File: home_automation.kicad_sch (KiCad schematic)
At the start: 44 parts, among them J1 AC In, J2 NodeMCU Header, J3 NodeMCU Header, J4 Conn_01x03_Male, J5 DHT11, J6 Conn_01x03_Male, J7 Conn_01x03_Male, J8 Conn_01x03_Male, K1 Relay_SPDT, K2 Relay_SPDT, K3 Relay_SPDT, K4 Relay_SPDT, Q1 D882_NPN_transistor, Q2 D882_NPN_transistor, Q3 D882_NPN_transistor, Q4 D882_NPN_transistor, U1 PC817, U2 PC817, U3 LM7805_TO220, U4 PC817, U5 PC817, U6 NodeMCU

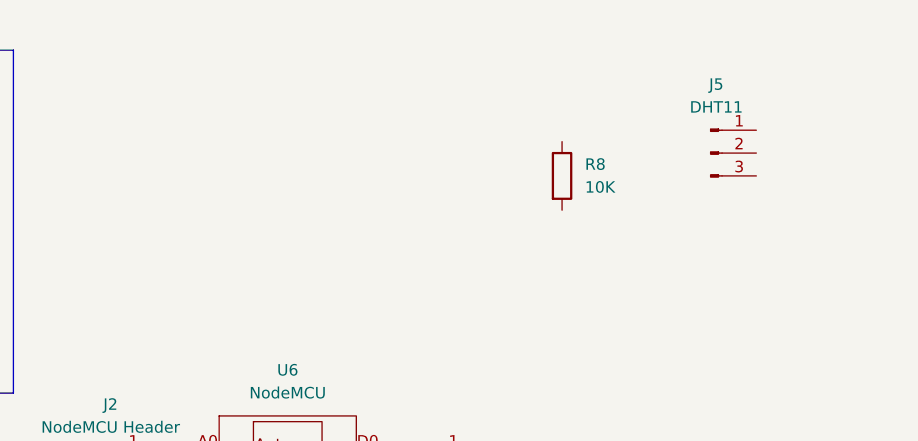
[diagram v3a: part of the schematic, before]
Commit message: DHT11 to NodeMCU  Wiring Completed
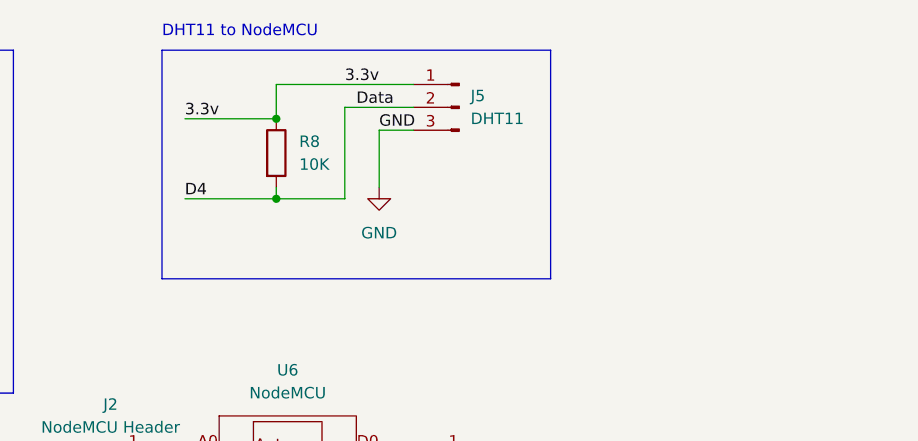
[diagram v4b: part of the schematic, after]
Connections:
- net GND: now also J5.3 (Pin_3)
- net 3.3v: now reaches J5.1 (Pin_1)
- net 3.3v: now also R8.1
- net D4: now reaches J5.2 (Pin_2)
- net D4: now also R8.2
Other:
- note added: "DHT11 to NodeMCU"
- moved on the sheet: J5, R8
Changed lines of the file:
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@@
     (rev "v1")
   )
+  (junction (at 203.2 25.4) (diameter 0) (color 0 0 0 0)
+  )
+  (junction (at 203.2 34.29) (diameter 0) (color 0 0 0 0)
+  )
   (junction (at 104.14 33.02) (diameter 0) (color 0 0 0 0)
   )
@@
     (stroke (width 0) (type default) (color 0 0 0 0))
   )
+  (wire (pts (xy 203.2 21.59) (xy 203.2 25.4))
+    (stroke (width 0) (type default) (color 0 0 0 0))
+  )
+  (polyline (pts (xy 190.5 17.78) (xy 233.68 17.78))
+    (stroke (width 0) (type default) (color 0 0 0 0))
+  )
   (wire (pts (xy 138.43 33.02) (xy 138.43 35.56))
     (stroke (width 0) (type default) (color 0 0 0 0))
   )
+  (wire (pts (xy 193.04 25.4) (xy 203.2 25.4))
+    (stroke (width 0) (type default) (color 0 0 0 0))
+  )
   (wire (pts (xy 104.14 33.02) (xy 115.57 33.02))
     (stroke (width 0) (type default) (color 0 0 0 0))
@@
     (stroke (width 0) (type default) (color 0 0 0 0))
   )
+  (wire (pts (xy 218.44 21.59) (xy 203.2 21.59))
+    (stroke (width 0) (type default) (color 0 0 0 0))
+  )
+  (polyline (pts (xy 233.68 17.78) (xy 233.68 43.18))
+    (stroke (width 0) (type default) (color 0 0 0 0))
+  )
   (polyline (pts (xy 92.71 17.78) (xy 92.71 55.88))
     (stroke (width 0) (type default) (color 0 0 0 0))
@@
     (stroke (width 0) (type default) (color 0 0 0 0))
   )
+  (wire (pts (xy 203.2 34.29) (xy 203.2 33.02))
+    (stroke (width 0) (type default) (color 0 0 0 0))
+  )
   (polyline (pts (xy 25.4 17.78) (xy 82.55 17.78))
     (stroke (width 0) (type default) (color 0 0 0 0))
@@
     (stroke (width 0) (type default) (color 0 0 0 0))
   )
+  (polyline (pts (xy 190.5 17.78) (xy 190.5 43.18))
+    (stroke (width 0) (type default) (color 0 0 0 0))
+  )
   (wire (pts (xy 104.14 43.18) (xy 104.14 48.26))
     (stroke (width 0) (type default) (color 0 0 0 0))
@@
     (stroke (width 0) (type default) (color 0 0 0 0))
   )
+  (wire (pts (xy 210.82 24.13) (xy 210.82 34.29))
+    (stroke (width 0) (type default) (color 0 0 0 0))
+  )
   (polyline (pts (xy 92.71 17.78) (xy 173.99 17.78))
     (stroke (width 0) (type default) (color 0 0 0 0))
   )
+  (wire (pts (xy 210.82 34.29) (xy 203.2 34.29))
+    (stroke (width 0) (type default) (color 0 0 0 0))
+  )
   (polyline (pts (xy 25.4 17.78) (xy 25.4 45.72))
     (stroke (width 0) (type default) (color 0 0 0 0))
@@
     (stroke (width 0) (type default) (color 0 0 0 0))
   )
+  (wire (pts (xy 214.63 26.67) (xy 214.63 33.02))
+    (stroke (width 0) (type default) (color 0 0 0 0))
+  )
   (wire (pts (xy 34.29 31.75) (xy 39.37 31.75))
     (stroke (width 0) (type default) (color 0 0 0 0))
@@
     (stroke (width 0) (type default) (color 0 0 0 0))
   )
+  (wire (pts (xy 193.04 34.29) (xy 203.2 34.29))
+    (stroke (width 0) (type default) (color 0 0 0 0))
+  )
+  (polyline (pts (xy 233.68 43.18) (xy 190.5 43.18))
+    (stroke (width 0) (type default) (color 0 0 0 0))
+  )
   (wire (pts (xy 160.02 25.4) (xy 165.1 25.4))
     (stroke (width 0) (type default) (color 0 0 0 0))
@@
     (stroke (width 0) (type default) (color 0 0 0 0))
   )
+  (wire (pts (xy 218.44 26.67) (xy 214.63 26.67))
+    (stroke (width 0) (type default) (color 0 0 0 0))
+  )
   (wire (pts (xy 104.14 48.26) (xy 123.19 48.26))
     (stroke (width 0) (type default) (color 0 0 0 0))
@@
     (stroke (width 0) (type default) (color 0 0 0 0))
   )
+  (wire (pts (xy 218.44 24.13) (xy 210.82 24.13))
+    (stroke (width 0) (type default) (color 0 0 0 0))
+  )
   (text "Power Input\n" (at 25.4 16.51 0)
     (effects (font (size 1.27 1.27)) (justify left bottom))
@@
     (effects (font (size 1.27 1.27)) (justify left bottom))
   )
+  (text "DHT11 to NodeMCU\n" (at 190.5 16.51 0)
+    (effects (font (size 1.27 1.27)) (justify left bottom))
+  )
   (label "12v" (at 71.12 27.94 0)
     (effects (font (size 1.27 1.27)) (justify left bottom))
@@
     (effects (font (size 1.27 1.27)) (justify left bottom))
   )
+  (label "3.3v" (at 210.82 21.59 0)
+    (effects (font (size 1.27 1.27)) (justify left bottom))
+  )
+  (label "3.3v" (at 193.04 25.4 0)
+    (effects (font (size 1.27 1.27)) (justify left bottom))
+  )
   (label "GND" (at 118.11 48.26 0)
     (effects (font (size 1.27 1.27)) (justify left bottom))
@@
   )
   (label "12v" (at 97.79 33.02 0)
+    (effects (font (size 1.27 1.27)) (justify left bottom))
+  )
+  (label "D4" (at 193.04 34.29 0)
+    (effects (font (size 1.27 1.27)) (justify left bottom))
+  )
+  (label "GND" (at 214.63 26.67 0)
+    (effects (font (size 1.27 1.27)) (justify left bottom))
+  )
+  (label "Data" (at 212.09 24.13 0)
     (effects (font (size 1.27 1.27)) (justify left bottom))
   )
@@
     (pin "2")
   )
-  (symbol (lib_id "Connector:Conn_01x03_Male") (at 251.46 29.21 0) (unit 1)
-    (in_bom yes) (on_board yes) (fields_autoplaced)
-    (property "Reference" "J5" (id 0) (at 252.095 21.59 0))
-    (property "Value" "DHT11 " (id 1) (at 252.095 24.13 0))
-    (property "Footprint" "" (id 2) (at 251.46 29.21 0)
-      (effects (font (size 1.27 1.27)) hide)
-    )
-    (property "Datasheet" "~" (id 3) (at 251.46 29.21 0)
+  (symbol (lib_id "Connector:Conn_01x03_Male") (at 223.52 24.13 0) (mirror y) (unit 1)
+    (in_bom yes) (on_board yes) (fields_autoplaced)
+    (property "Reference" "J5" (id 0) (at 224.79 22.8599 0)
+      (effects (font (size 1.27 1.27)) (justify right))
+    )
+    (property "Value" "DHT11 " (id 1) (at 224.79 25.3999 0)
+      (effects (font (size 1.27 1.27)) (justify right))
+    )
+    (property "Footprint" "" (id 2) (at 223.52 24.13 0)
+      (effects (font (size 1.27 1.27)) hide)
+    )
+    (property "Datasheet" "~" (id 3) (at 223.52 24.13 0)
       (effects (font (size 1.27 1.27)) hide)
     )
@@
     (pin "3")
     (pin "4")
+  )
+  (symbol (lib_id "power:GND") (at 214.63 33.02 0) (unit 1)
+    (in_bom yes) (on_board yes) (fields_autoplaced)
+    (property "Reference" "#PWR?" (id 0) (at 214.63 39.37 0)
+      (effects (font (size 1.27 1.27)) hide)
+    )
+    (property "Value" "GND" (id 1) (at 214.63 38.1 0))
+    (property "Footprint" "" (id 2) (at 214.63 33.02 0)
+      (effects (font (size 1.27 1.27)) hide)
+    )
+    (property "Datasheet" "" (id 3) (at 214.63 33.02 0)
+      (effects (font (size 1.27 1.27)) hide)
+    )
+    (pin "1")
   )
   (symbol (lib_id "Relay_SPDT:Relay_SPDT") (at 85.09 142.24 0) (unit 1)
@@
     (pin "Vin")
   )
-  (symbol (lib_id "Device:R") (at 234.95 31.75 0) (unit 1)
-    (in_bom yes) (on_board yes) (fields_autoplaced)
-    (property "Reference" "R8" (id 0) (at 237.49 30.4799 0)
-      (effects (font (size 1.27 1.27)) (justify left))
-    )
-    (property "Value" "10K" (id 1) (at 237.49 33.0199 0)
-      (effects (font (size 1.27 1.27)) (justify left))
-    )
-    (property "Footprint" "" (id 2) (at 233.172 31.75 90)
-      (effects (font (size 1.27 1.27)) hide)
-    )
-    (property "Datasheet" "~" (id 3) (at 234.95 31.75 0)
+  (symbol (lib_id "Device:R") (at 203.2 29.21 0) (unit 1)
+    (in_bom yes) (on_board yes) (fields_autoplaced)
+    (property "Reference" "R8" (id 0) (at 205.74 27.9399 0)
+      (effects (font (size 1.27 1.27)) (justify left))
+    )
+    (property "Value" "10K" (id 1) (at 205.74 30.4799 0)
+      (effects (font (size 1.27 1.27)) (justify left))
+    )
+    (property "Footprint" "" (id 2) (at 201.422 29.21 90)
+      (effects (font (size 1.27 1.27)) hide)
+    )
+    (property "Datasheet" "~" (id 3) (at 203.2 29.21 0)
       (effects (font (size 1.27 1.27)) hide)
     )
@@
       (reference "#PWR?") (unit 1) (value "GND") (footprint "")
     )
+    (path "/c48563d9-5f2a-49d7-82a6-9b945544f3a5"
+      (reference "#PWR?") (unit 1) (value "GND") (footprint "")
+    )

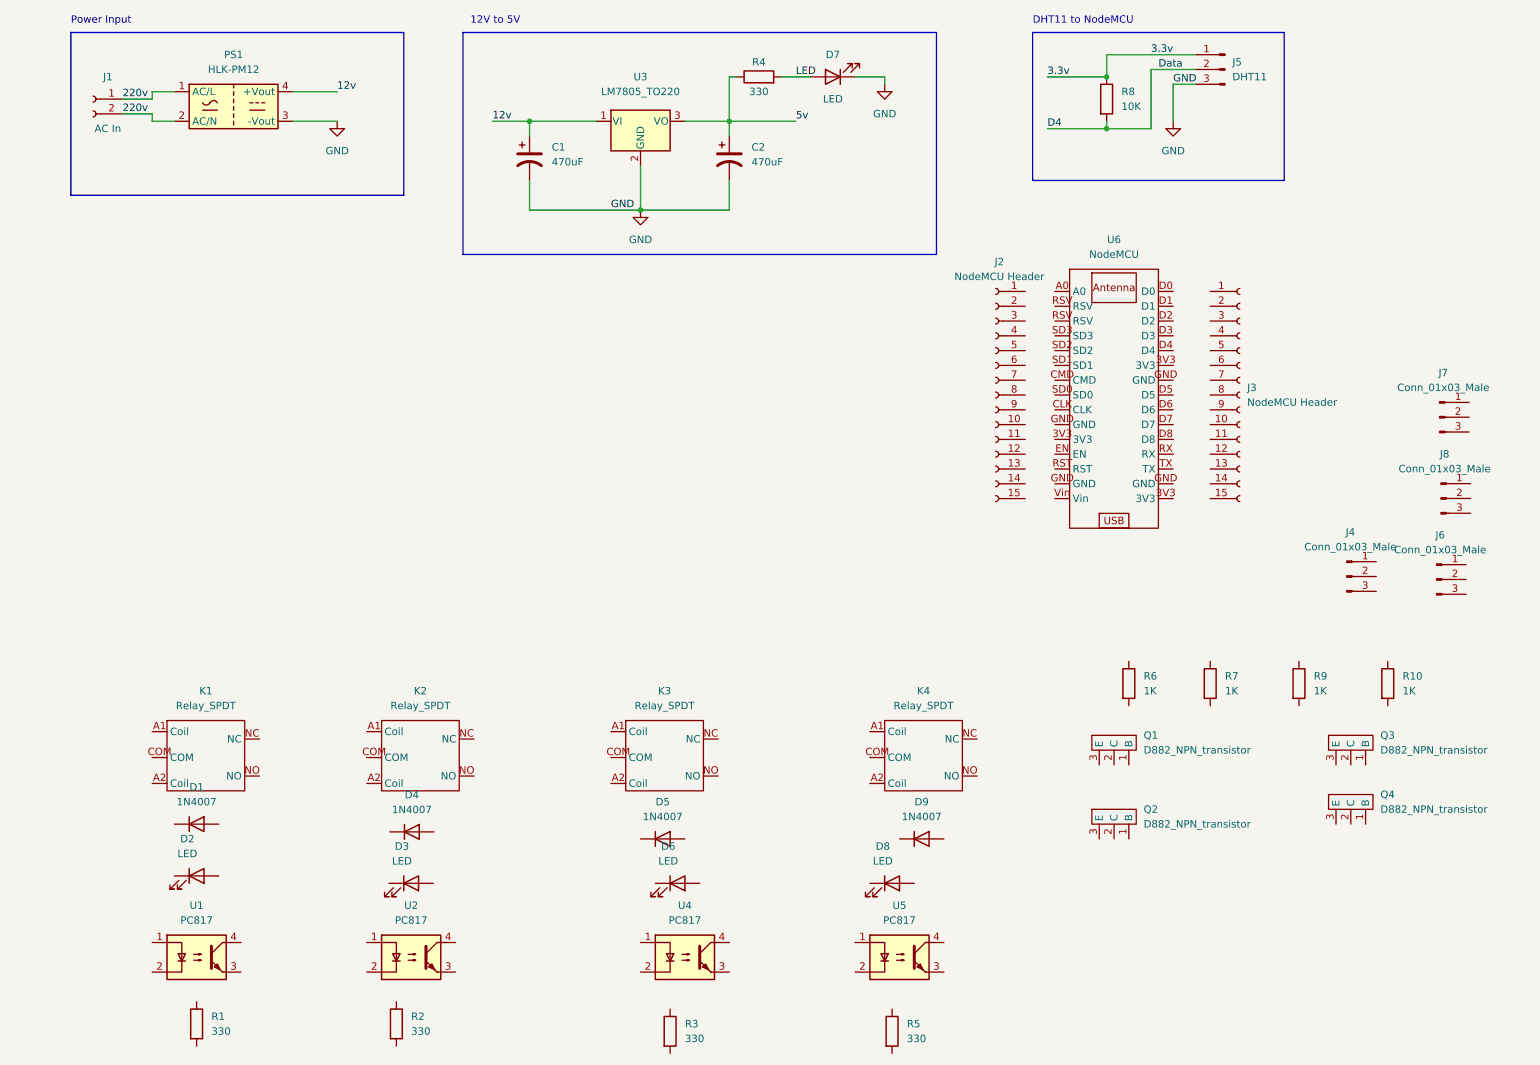
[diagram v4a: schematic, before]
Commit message: Relay wiring completed
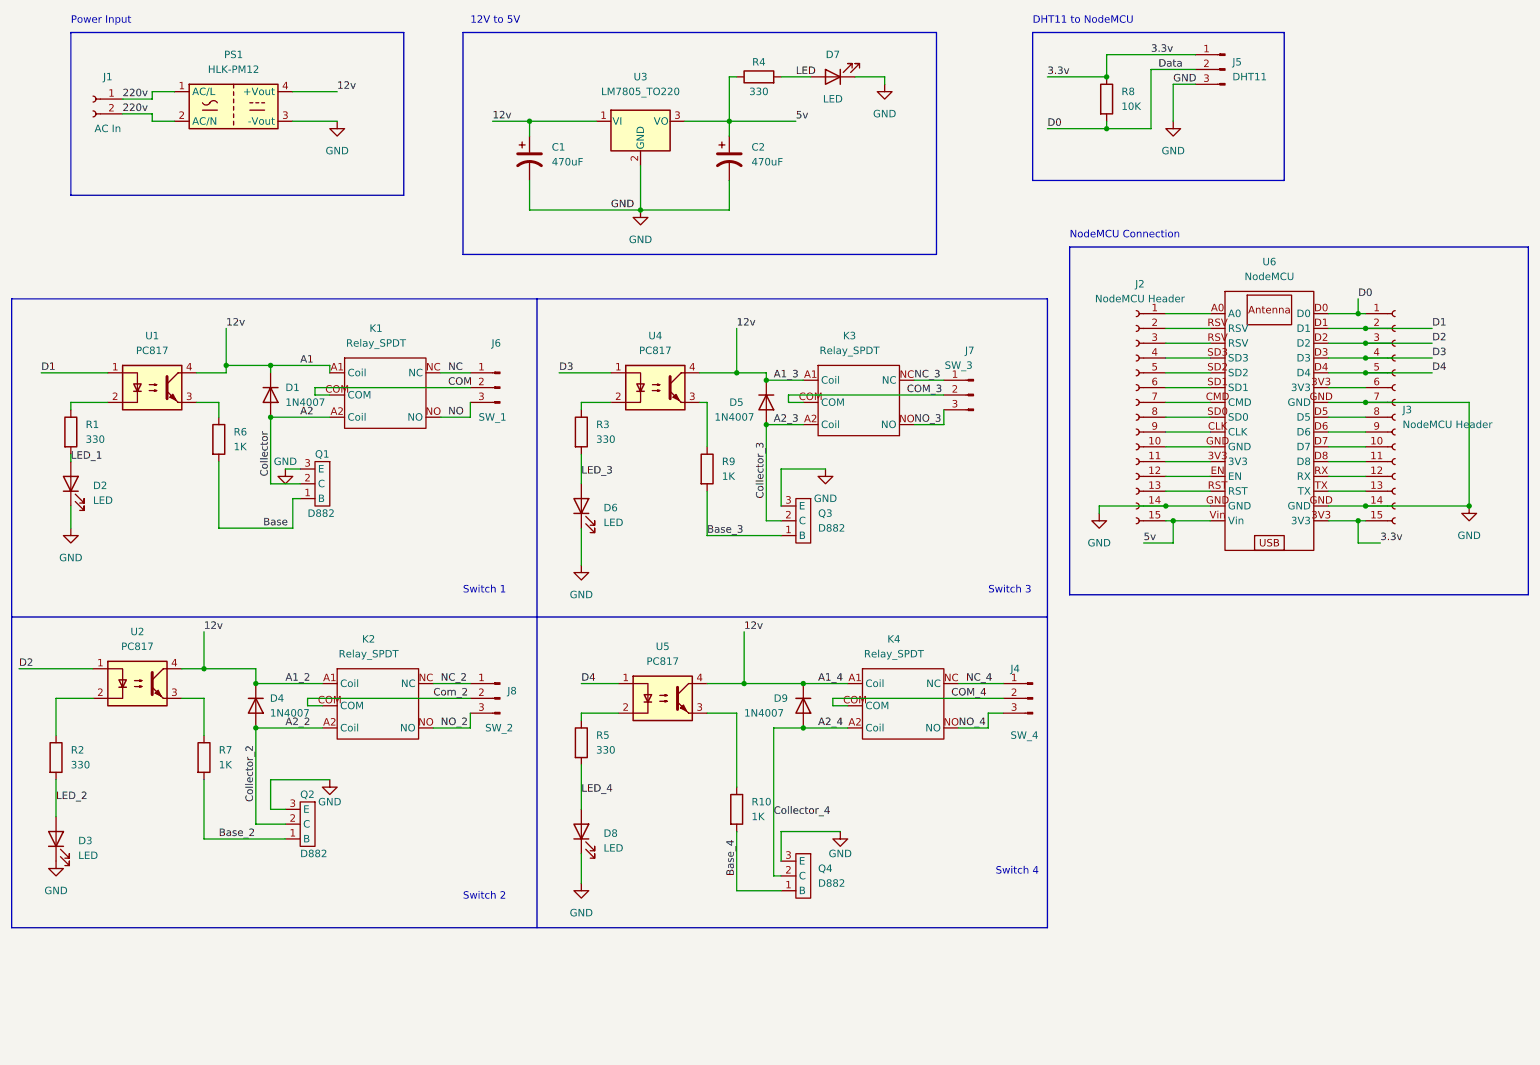
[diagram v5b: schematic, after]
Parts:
- J4: value Conn_01x03_Male -> SW_4
- J6: value Conn_01x03_Male -> SW_1
- J7: value Conn_01x03_Male -> SW_3
- J8: value Conn_01x03_Male -> SW_2
- Q1, Q2, Q3, Q4: value D882_NPN_transistor -> D882
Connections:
- net 12v: now also D1.1 (K), D4.1 (K), D5.1 (K), D9.1 (K), K1.A1 (Coil), K2.A1 (Coil), K3.A1 (Coil), K4.A1 (Coil), U1.4, U2.4, U4.4, U5.4
- net 3.3v: now also J3.15 (Pin_15), U6.3V3
- net 5v: now also J2.15 (Pin_15), U6.Vin
- net D4: now also J3.5 (Pin_5), U5.1, U6.D4; no longer J5.2 (Pin_2), R8.2
- net GND: now also D2.1 (K), D3.1 (K), D6.1 (K), D8.1 (K), J2.14 (Pin_14), J3.14 (Pin_14), J3.7 (Pin_7), Q1.3 (E), Q2.3 (E), Q3.3 (E), Q4.3 (E), U6.GND
- net Base_4: now reaches Q4.1 (B)
- net Base_4: now also R10.2
- net A2_4: now reaches Q4.2 (C)
- net A2_4: now also D9.2 (A), K4.A2 (Coil)
- net D2: now reaches U2.1
- net D2: now also J3.3 (Pin_3), U6.D2
- net at U2.2: now also R2.1
- net at U2.3: now also R7.1
- net LED_1: now reaches D2.2 (A)
- net LED_1: now also R1.2
- net LED_2: now reaches D3.2 (A)
- net LED_2: now also R2.2
- net at R3.1: now also U4.2
- net LED_3: now reaches R3.2
- net LED_3: now also D6.2 (A)
- net Base_2: now reaches Q2.1 (B)
- net Base_2: now also R7.2
- net A2_2: now reaches Q2.2 (C)
- net A2_2: now also D4.2 (A), K2.A2 (Coil)
- net at J2.1 (Pin_1): now also U6.A0
- net at J2.10 (Pin_10): now also U6.GND
- net at J2.11 (Pin_11): now also U6.3V3
- net at J2.12 (Pin_12): now also U6.EN
- net at J2.13 (Pin_13): now also U6.RST
- net at J2.2 (Pin_2): now also U6.RSV
- net at J2.3 (Pin_3): now also U6.RSV
- net at J2.4 (Pin_4): now also U6.SD3
- net at J2.5 (Pin_5): now also U6.SD2
- net at J2.6 (Pin_6): now also U6.SD1
- net at J2.7 (Pin_7): now also U6.CMD
- net at J2.8 (Pin_8): now also U6.SD0
- net at J2.9 (Pin_9): now also U6.CLK
- net NC: now reaches J6.1 (Pin_1)
- net NC: now also K1.NC
- net COM: now reaches J6.2 (Pin_2)
- net COM: now also K1.COM
- net NO: now reaches J6.3 (Pin_3)
- net NO: now also K1.NO
- net LED_4: now reaches D8.2 (A)
- net LED_4: now also R5.2
- net A2_3: now reaches K3.A2 (Coil)
- net A2_3: now also D5.2 (A), Q3.2 (C)
- net COM_3: now reaches K3.COM
- net COM_3: now also J7.2 (Pin_2)
- net NC_3: now reaches K3.NC
- net NC_3: now also J7.1 (Pin_1)
- net NO_3: now reaches K3.NO
- net NO_3: now also J7.3 (Pin_3)
- net at U5.2: now also R5.1
- net at U5.3: now also R10.1
- net D3: now reaches U4.1
- net D3: now also J3.4 (Pin_4), U6.D3
- net at U4.3: now also R9.1
- net D0: now reaches J3.1 (Pin_1)
- net D0: now also J5.2 (Pin_2), R8.2, U6.D0
- net at J3.10 (Pin_10): now also U6.D7
- net at J3.11 (Pin_11): now also U6.D8
- net at J3.12 (Pin_12): now also U6.RX
- net at J3.13 (Pin_13): now also U6.TX
- net D1: now reaches J3.2 (Pin_2)
- net D1: now also U1.1, U6.D1
- net at J3.6 (Pin_6): now also U6.3V3
- net at J3.8 (Pin_8): now also U6.D5
- net at J3.9 (Pin_9): now also U6.D6
- net at R1.1: now also U1.2
- net at R6.1: now also U1.3
- net Base: now reaches R6.2
- net Base: now also Q1.1 (B)
- net A2: now reaches Q1.2 (C)
- net A2: now also D1.2 (A), K1.A2 (Coil)
- net NC_4: now reaches J4.1 (Pin_1)
- net NC_4: now also K4.NC
- net COM_4: now reaches J4.2 (Pin_2)
- net COM_4: now also K4.COM
- net NO_4: now reaches J4.3 (Pin_3)
- net NO_4: now also K4.NO
- net NC_2: now reaches J8.1 (Pin_1)
- net NC_2: now also K2.NC
- net Com_2: now reaches J8.2 (Pin_2)
- net Com_2: now also K2.COM
- net NO_2: now reaches J8.3 (Pin_3)
- net NO_2: now also K2.NO
- net Base_3: now reaches R9.2
- net Base_3: now also Q3.1 (B)
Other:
- note added: "NodeMCU Connection"
- note added: "Switch 1"
- note added: "Switch 2"
- note added: "Switch 3"
- note added: "Switch 4"
- moved on the sheet: D1, D2, D3, D4, D5, D6, D8, D9, J2, J3, J4, J6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
